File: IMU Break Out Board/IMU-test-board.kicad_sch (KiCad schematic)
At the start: 12 parts, among them J1 Conn_01x04, J2 Conn_01x03, U1 BMI088, U2 LSM6DSOTR, U3 LSM303AGRTR

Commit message: edits
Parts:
- added R3: 200, Resistor_SMD:R_0603_1608Metric, symbol Device:R
- D1: footprint LED_SMD:LED_0201_0603Metric -> LED_SMD:LED_0603_1608Metric
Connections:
- net +3.3V: now also R3.1; no longer D1.2 (A)
- new net: D1.2 (A), R3.2
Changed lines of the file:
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@@
+	(wire
+		(pts
+			(xy 232.41 67.31) (xy 233.68 67.31)
+		)
+		(stroke
+			(width 0)
+			(type default)
+		)
+	)
 	(wire
 		(pts
@@
 			)
 		)
-		(property "Footprint" "LED_SMD:LED_0201_0603Metric"
+		(property "Footprint" "LED_SMD:LED_0603_1608Metric"
 			(at 237.49 67.31 0)
 			(hide yes)
@@
 	(symbol
 		(lib_id "power:+3.3V")
-		(at 233.68 67.31 90)
+		(at 224.79 67.31 90)
 		(unit 1)
 		(body_style 1)
@@
 		(fields_autoplaced yes)
 		(property "Reference" "#PWR022"
-			(at 237.49 67.31 0)
+			(at 228.6 67.31 0)
 			(hide yes)
 			(show_name no)
@@
 		)
 		(property "Value" "+3.3V"
-			(at 229.87 67.3099 90)
+			(at 220.98 67.3099 90)
 			(show_name no)
 			(do_not_autoplace no)
@@
 		)
 		(property "Footprint" ""
-			(at 233.68 67.31 0)
+			(at 224.79 67.31 0)
 			(hide yes)
 			(show_name no)
@@
 		)
 		(property "Datasheet" ""
-			(at 233.68 67.31 0)
+			(at 224.79 67.31 0)
 			(hide yes)
 			(show_name no)
@@
 		)
 		(property "Description" "Power symbol creates a global label with name \"+3.3V\""
-			(at 233.68 67.31 0)
+			(at 224.79 67.31 0)
 			(hide yes)
 			(show_name no)
@@
 					(unit 1)
 				)
+			)
+		)
+	)
+	(symbol
+		(lib_id "Device:R")
+		(at 228.6 67.31 90)
+		(unit 1)
+		(body_style 1)
+		(exclude_from_sim no)
+		(in_bom yes)
+		(on_board yes)
+		(in_pos_files yes)
+		(dnp no)
+		(fields_autoplaced yes)
+		(property "Reference" "R3"
+			(at 228.6 60.96 90)
+			(show_name no)
+			(do_not_autoplace no)
+			(effects
+				(font
+					(size 1.27 1.27)
+				)
+			)
+		)
+		(property "Value" "200"
+			(at 228.6 63.5 90)
+			(show_name no)
+			(do_not_autoplace no)
+			(effects
+				(font
+					(size 1.27 1.27)
+				)
+			)
+		)
+		(property "Footprint" "Resistor_SMD:R_0603_1608Metric"
+			(at 228.6 69.088 90)
+			(hide yes)
+			(show_name no)
+			(do_not_autoplace no)
+			(effects
+				(font
+					(size 1.27 1.27)
+				)
+			)
+		)
+		(property "Datasheet" ""
+			(at 228.6 67.31 0)
+			(hide yes)
+			(show_name no)
+			(do_not_autoplace no)
+			(effects
+				(font
+					(size 1.27 1.27)
+				)
+			)
+		)
+		(property "Description" "Resistor"
+			(at 228.6 67.31 0)
+			(hide yes)
+			(show_name no)
+			(do_not_autoplace no)
+			(effects
+				(font
+					(size 1.27 1.27)
+				)
+			)
+		)
+		(pin "2"
+		)
+		(pin "1"
+		)
+		(instances
+			(project "IMU-test-board"
+				(path "/3ea5a38f-3abe-4456-b6d4-eace866449fb"
+					(reference "R3")
+					(unit 1)
+				)

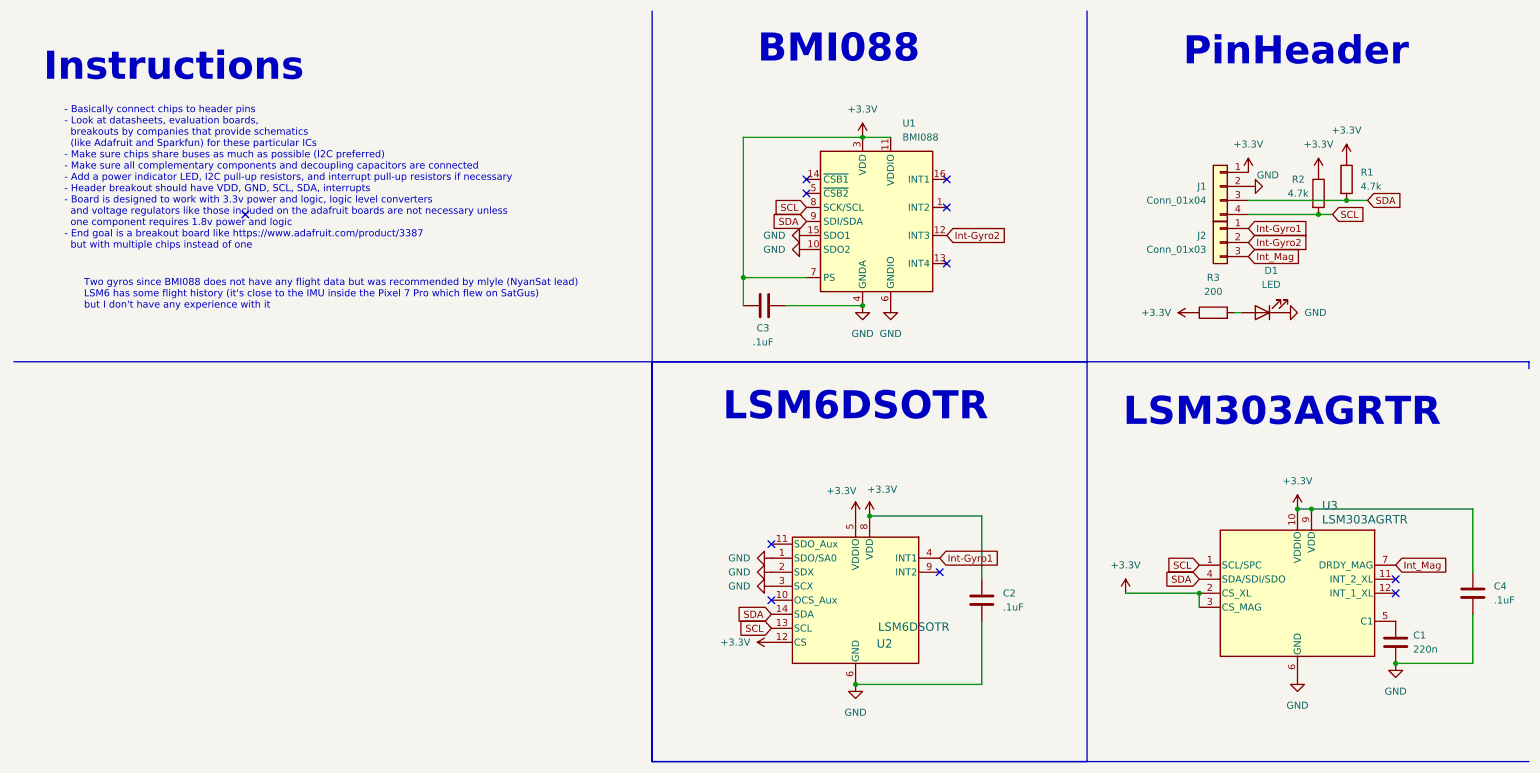
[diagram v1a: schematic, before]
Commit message: Clean up IMU board and make it breadboard compatible
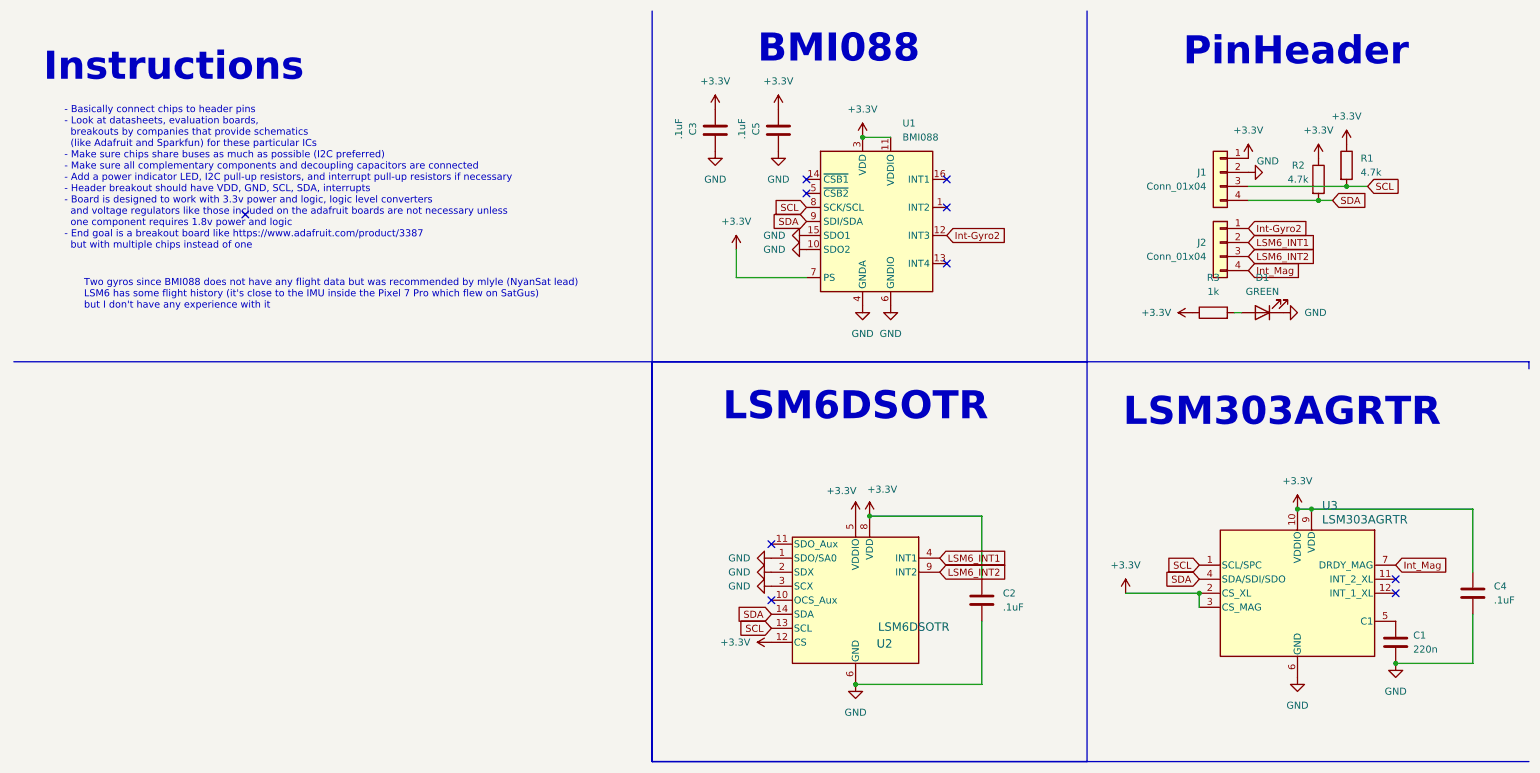
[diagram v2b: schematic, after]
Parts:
- removed J2: Conn_01x03, Connector_PinHeader_2.54mm:PinHeader_1x03_P2.54mm_Vertical, symbol Connector_Generic:Conn_01x03
- added C5: .1uF, Capacitor_SMD:C_0603_1608Metric, symbol Device:C
- added J2: Conn_01x04, Connector_PinHeader_2.54mm:PinHeader_1x04_P2.54mm_Vertical, symbol Connector_Generic:Conn_01x04
- D1: value LED -> GREEN
- R3: value 200 -> 1k
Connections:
- net +3.3V: now also C5.1
- net GND: now also C5.2
- net Int-Gyro2: now also J2.1 (Pin_1)
- net Int_Mag: now also J2.4 (Pin_4)
- net SCL: now also J1.3 (Pin_3), R1.2; no longer J1.4 (Pin_4), R2.2
- net SDA: now also J1.4 (Pin_4), R2.2; no longer J1.3 (Pin_3), R1.2
- net LSM6_INT2: now reaches U2.9 (INT2)
- net LSM6_INT2: now also J2.3 (Pin_3)
- net Int-Gyro1 renamed LSM6_INT1
- net LSM6_INT1: now also J2.2 (Pin_2)
- no-connect marks 11 -> 10
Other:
- moved on the sheet: C3, J1, R1, R2
